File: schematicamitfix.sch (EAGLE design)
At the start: 39 parts, among them J1 FTDI_DEVICE, M1 WIRELESS-NRF24L01, U1 ATMEGA328P_TQFP, U2 GY-521MPU6050, U3 MAX1595EUA33+, Y1 8MHz

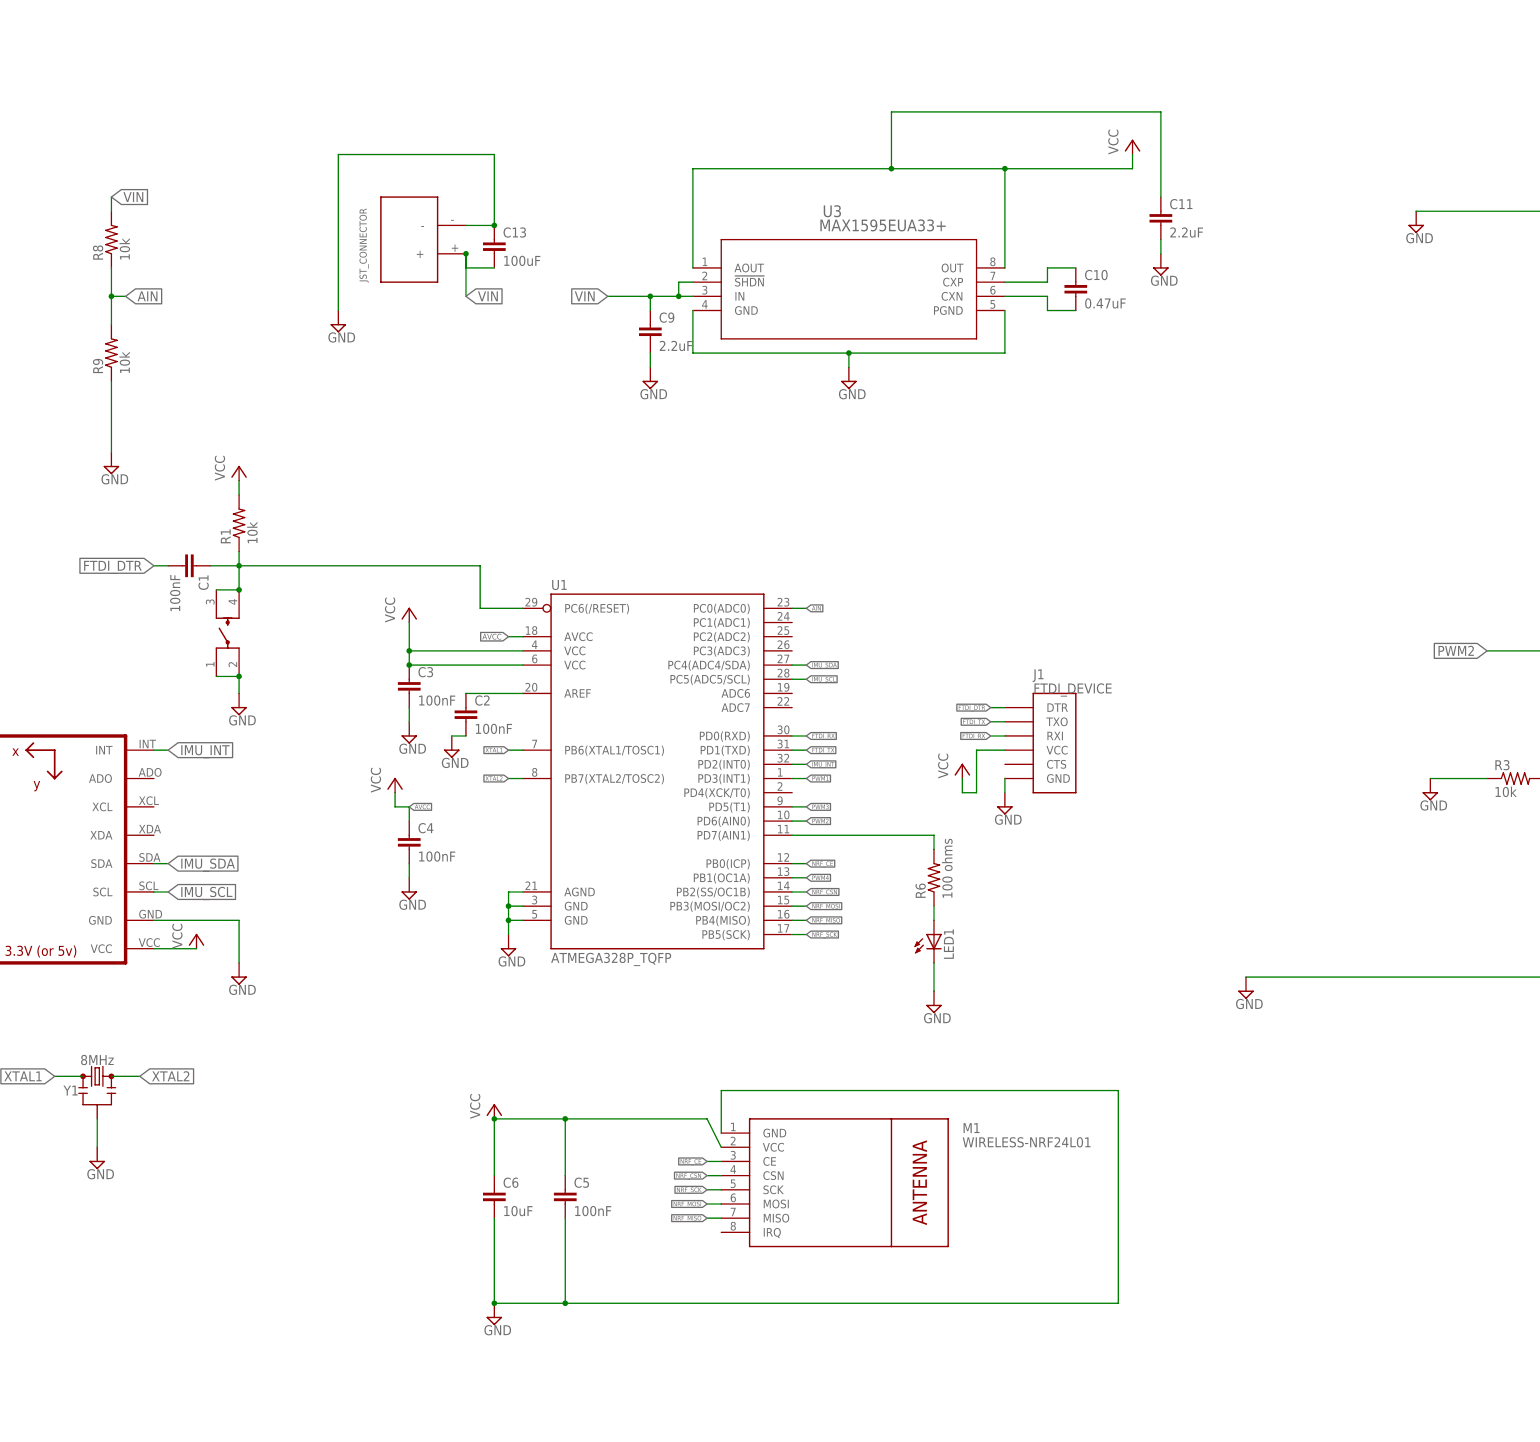
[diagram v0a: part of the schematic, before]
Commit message: Fixed ERC warnings about VCC and GND
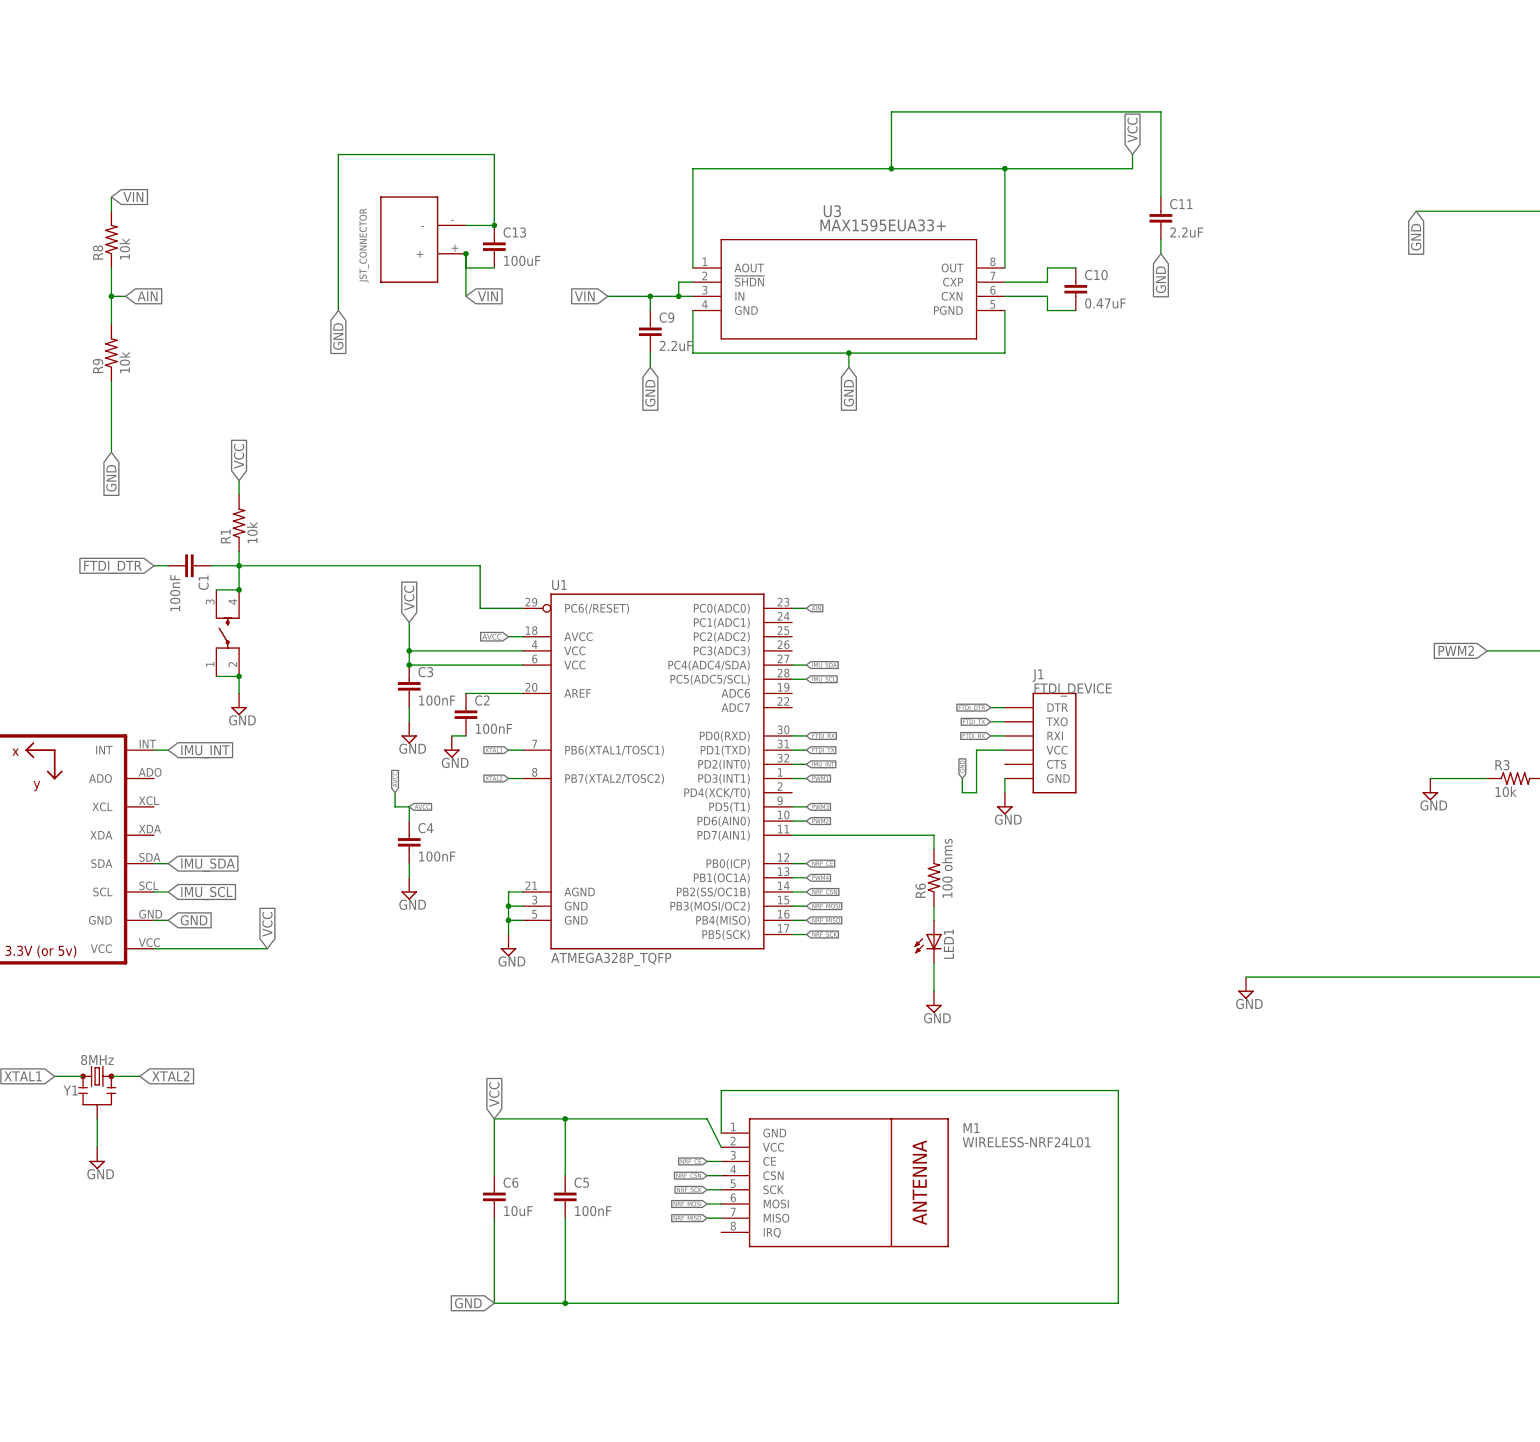
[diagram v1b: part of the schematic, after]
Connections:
- net GND: now also J1.VCC
- net VCC: no longer J1.VCC

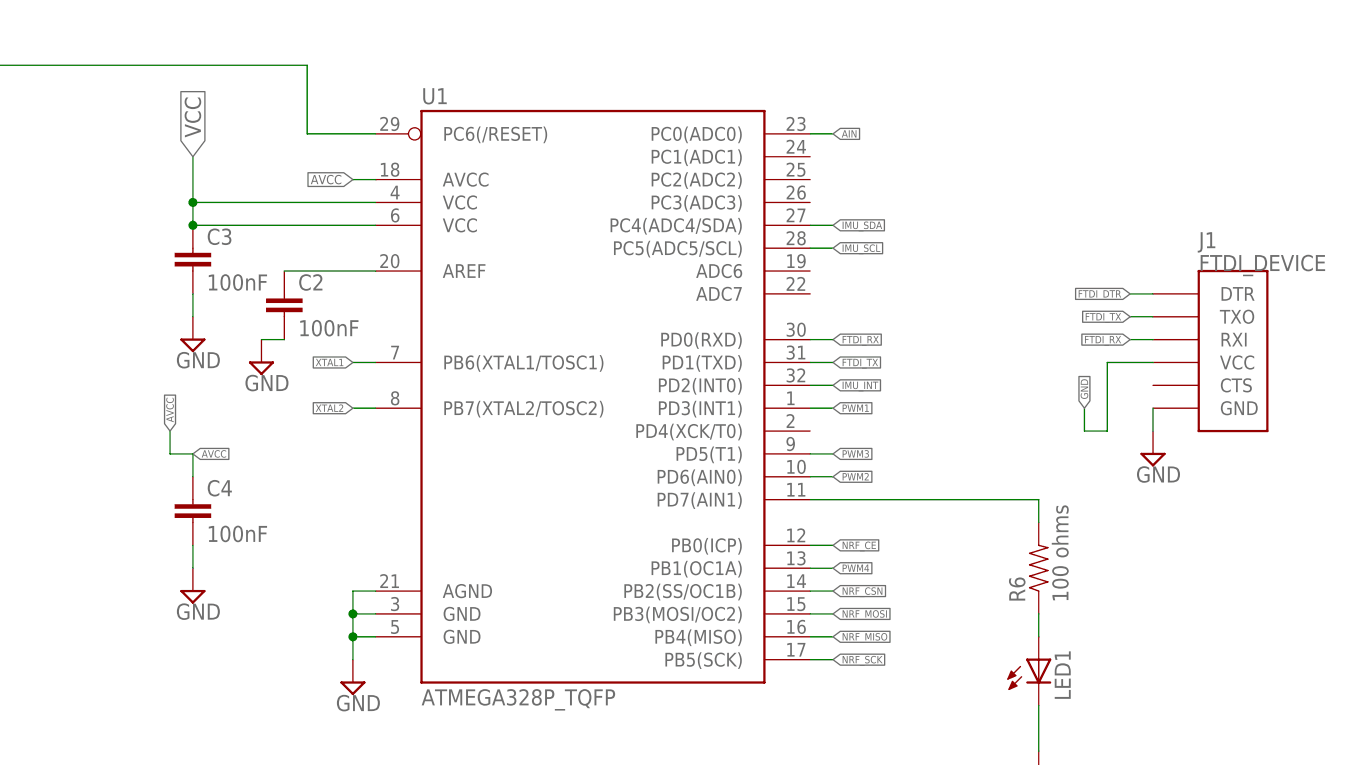
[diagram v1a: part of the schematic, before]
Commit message: Modified LED Resistor value
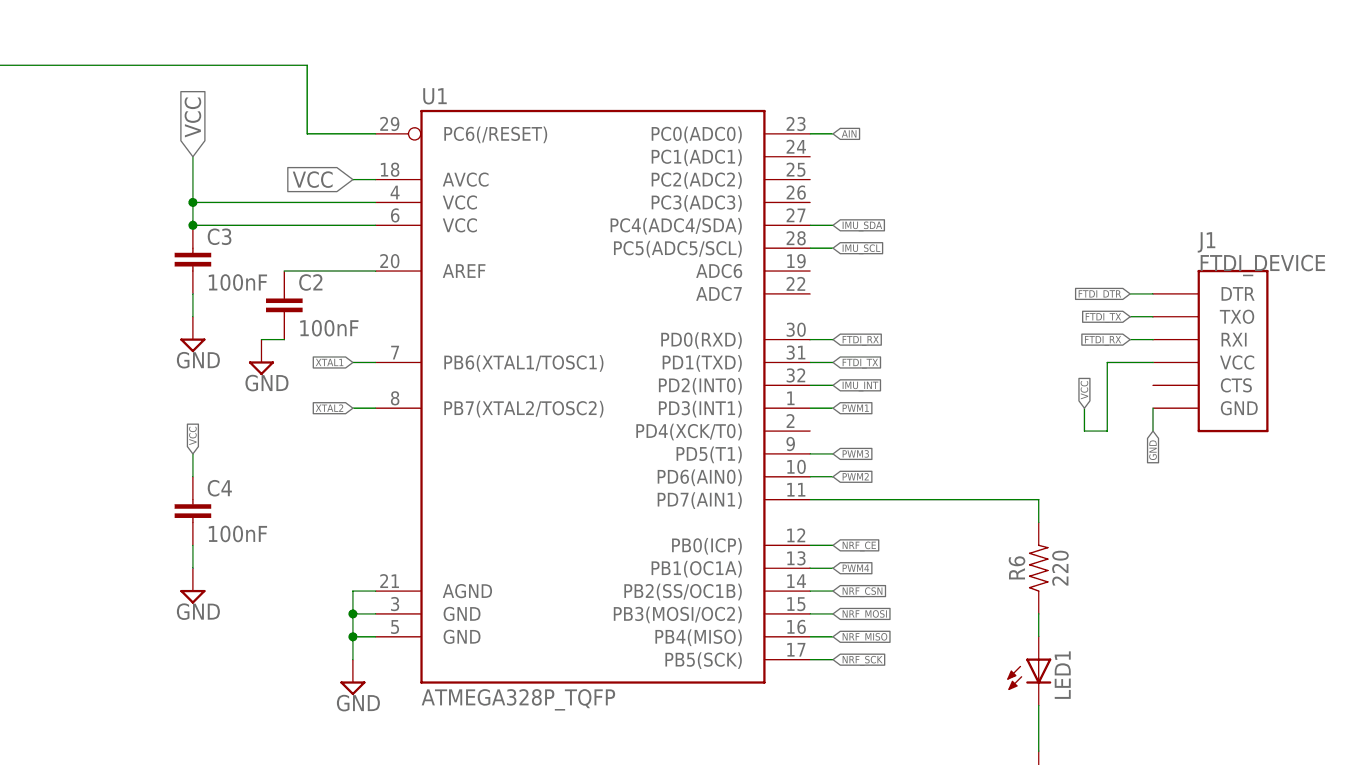
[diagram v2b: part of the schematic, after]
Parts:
- R6: value 100 ohms -> 220; device SparkFun:RESISTOR0603-RES -> SparkFun-Resistors:220OHM-0603-1/10W-1%
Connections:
- removed net AVCC: C4.1, U1.AVCC
- net GND: no longer J1.VCC
- net VCC: now also C4.1, J1.VCC, U1.AVCC
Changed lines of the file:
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@@
 <part name="U2" library="quad" deviceset="GY-521" device="MPU6050"/>
 <part name="M1" library="quad" deviceset="WIRELESS-NRF24L01" device=""/>
-<part name="SUPPLY2" library="supply2" library_urn="urn:adsk.eagle:library:372" deviceset="GND" device=""/>
 <part name="SUPPLY5" library="supply2" library_urn="urn:adsk.eagle:library:372" deviceset="GND" device=""/>
 <part name="SUPPLY6" library="supply2" library_urn="urn:adsk.eagle:library:372" deviceset="GND" device=""/>
@@
 <part name="R5" library="SparkFun-Resistors" deviceset="RESISTOR" device="0603" value="10k"/>
 <part name="LED1" library="LilyPad-Wearables" deviceset="LED" device="1206"/>
-<part name="R6" library="SparkFun" deviceset="RESISTOR" device="0603-RES" value="100 ohms"/>
 <part name="U$19" library="quad" deviceset="JST_CONNECTOR_FEMALE" device=""/>
 <part name="SUPPLY16" library="supply2" library_urn="urn:adsk.eagle:library:372" deviceset="GND" device=""/>
@@
 <part name="Y1" library="SparkFun-Clocks" deviceset="RESONATOR-8MHZ" device="SMD_3.2X1.3" value="8MHz"/>
 <part name="SUPPLY13" library="supply2" library_urn="urn:adsk.eagle:library:372" deviceset="GND" device=""/>
+<part name="R6" library="SparkFun-Resistors" deviceset="220OHM" device="-0603-1/10W-1%" value="220"/>
 </parts>
 <sheets>
@@
 <instance part="U2" gate="G$1" x="-43.18" y="22.86" rot="R180"/>
 <instance part="M1" gate="G$1" x="96.52" y="-35.56"/>
-<instance part="SUPPLY2" gate="GND" x="124.46" y="33.02"/>
 <instance part="SUPPLY5" gate="GND" x="35.56" y="7.62"/>
 <instance part="SUPPLY6" gate="GND" x="25.4" y="43.18"/>
@@
 <instance part="R5" gate="G$1" x="185.42" y="-254" rot="R90"/>
 <instance part="LED1" gate="G$1" x="111.76" y="10.16"/>
-<instance part="R6" gate="G$1" x="111.76" y="20.32" rot="R90"/>
 <instance part="U$19" gate="G$1" x="17.78" y="134.62" rot="R90"/>
 <instance part="SUPPLY16" gate="GND" x="264.16" y="236.22"/>
@@
 <instance part="Y1" gate="G$1" x="-38.1" y="-15.24"/>
 <instance part="SUPPLY13" gate="GND" x="-38.1" y="-30.48"/>
+<instance part="R6" gate="G$1" x="111.76" y="20.32" rot="R90"/>
 </instances>
 <busses>
@@
 </segment>
 <segment>
-<pinref part="J1" gate="G$1" pin="GND"/>
-<wire x1="124.46" y1="38.1" x2="124.46" y2="35.56" width="0.1524" layer="91"/>
-<pinref part="SUPPLY2" gate="GND" pin="GND"/>
-</segment>
-<segment>
 <wire x1="60.96" y1="114.3" x2="60.96" y2="111.76" width="0.1524" layer="91"/>
 <pinref part="C9" gate="G$1" pin="2"/>
@@
 </segment>
 <segment>
-<pinref part="J1" gate="G$1" pin="VCC"/>
-<wire x1="124.46" y1="43.18" x2="119.38" y2="43.18" width="0.1524" layer="91"/>
-<wire x1="119.38" y1="43.18" x2="119.38" y2="35.56" width="0.1524" layer="91"/>
-<wire x1="119.38" y1="35.56" x2="116.84" y2="35.56" width="0.1524" layer="91"/>
-<wire x1="116.84" y1="35.56" x2="116.84" y2="38.1" width="0.1524" layer="91"/>
-<label x="116.84" y="38.1" size="0.8128" layer="95" rot="R90" xref="yes"/>
+<pinref part="J1" gate="G$1" pin="GND"/>
+<wire x1="124.46" y1="38.1" x2="124.46" y2="35.56" width="0.1524" layer="91"/>
+<label x="124.46" y="35.56" size="0.8128" layer="95" rot="R270" xref="yes"/>
 </segment>
 </net>
@@
 <wire x1="-27.94" y1="7.62" x2="-7.62" y2="7.62" width="0.1524" layer="91"/>
 <label x="-7.62" y="7.62" size="1.778" layer="95" rot="R90" xref="yes"/>
-</segment>
-<segment>
-<pinref part="U1" gate="U$1" pin="VCC@6"/>
-<wire x1="38.1" y1="58.42" x2="17.78" y2="58.42" width="0.1524" layer="91"/>
-<pinref part="U1" gate="U$1" pin="VCC@4"/>
-<wire x1="38.1" y1="60.96" x2="17.78" y2="60.96" width="0.1524" layer="91"/>
-<wire x1="17.78" y1="58.42" x2="17.78" y2="60.96" width="0.1524" layer="91"/>
-<junction x="17.78" y="60.96"/>
-<wire x1="17.78" y1="60.96" x2="17.78" y2="66.04" width="0.1524" layer="91"/>
-<pinref part="C3" gate="G$1" pin="1"/>
-<junction x="17.78" y="58.42"/>
-<label x="17.78" y="66.04" size="1.778" layer="95" rot="R90" xref="yes"/>
 </segment>
 <segment>
@@
 <label x="147.32" y="149.86" size="1.778" layer="95" rot="R90" xref="yes"/>
 </segment>
+<segment>
+<pinref part="U1" gate="U$1" pin="VCC@6"/>
+<wire x1="38.1" y1="58.42" x2="17.78" y2="58.42" width="0.1524" layer="91"/>
+<pinref part="U1" gate="U$1" pin="VCC@4"/>
+<wire x1="38.1" y1="60.96" x2="17.78" y2="60.96" width="0.1524" layer="91"/>
+<wire x1="17.78" y1="58.42" x2="17.78" y2="60.96" width="0.1524" layer="91"/>
+<junction x="17.78" y="60.96"/>
+<wire x1="17.78" y1="60.96" x2="17.78" y2="66.04" width="0.1524" layer="91"/>
+<pinref part="C3" gate="G$1" pin="1"/>
+<junction x="17.78" y="58.42"/>
+<label x="17.78" y="66.04" size="1.778" layer="95" rot="R90" xref="yes"/>
+</segment>
+<segment>
+<pinref part="U1" gate="U$1" pin="AVCC"/>
+<wire x1="38.1" y1="63.5" x2="35.56" y2="63.5" width="0.1524" layer="91"/>
+<label x="35.56" y="63.5" size="1.778" layer="95" rot="R180" xref="yes"/>
+</segment>
+<segment>
+<pinref part="C4" gate="G$1" pin="1"/>
+<wire x1="17.78" y1="30.48" x2="17.78" y2="33.02" width="0.1524" layer="91"/>
+<label x="17.78" y="33.02" size="0.8128" layer="95" rot="R90" xref="yes"/>
+</segment>
+<segment>
+<pinref part="J1" gate="G$1" pin="VCC"/>
+<wire x1="124.46" y1="43.18" x2="119.38" y2="43.18" width="0.1524" layer="91"/>
+<wire x1="119.38" y1="43.18" x2="119.38" y2="35.56" width="0.1524" layer="91"/>
+<wire x1="119.38" y1="35.56" x2="116.84" y2="35.56" width="0.1524" layer="91"/>
+<wire x1="116.84" y1="35.56" x2="116.84" y2="38.1" width="0.1524" layer="91"/>
+<label x="116.84" y="38.1" size="0.8128" layer="95" rot="R90" xref="yes"/>
+</segment>
 </net>
 <net name="FTDI_TX" class="0">
@@
 </segment>
 </net>
-<net name="AVCC" class="0">
-<segment>
-<pinref part="U1" gate="U$1" pin="AVCC"/>
-<wire x1="38.1" y1="63.5" x2="35.56" y2="63.5" width="0.1524" layer="91"/>
-<label x="35.56" y="63.5" size="1.016" layer="95" rot="R180" xref="yes"/>
-</segment>
-<segment>
-<pinref part="C4" gate="G$1" pin="1"/>
-<wire x1="17.78" y1="30.48" x2="17.78" y2="33.02" width="0.1524" layer="91"/>
-<label x="17.78" y="33.02" size="0.8128" layer="95" xref="yes"/>
-<wire x1="17.78" y1="33.02" x2="15.24" y2="33.02" width="0.1524" layer="91"/>
-<wire x1="15.24" y1="33.02" x2="15.24" y2="35.56" width="0.1524" layer="91"/>
-<label x="15.24" y="35.56" size="0.8128" layer="95" rot="R90" xref="yes"/>
-</segment>
-</net>
 <net name="PWM2" class="0">
 <segment>
@@
 <net name="N$7" class="0">
 <segment>
-<pinref part="R6" gate="G$1" pin="2"/>
 <wire x1="111.76" y1="27.94" x2="111.76" y2="25.4" width="0.1524" layer="91"/>
 <pinref part="U1" gate="U$1" pin="PD7(AIN1)"/>
 <wire x1="111.76" y1="27.94" x2="86.36" y2="27.94" width="0.1524" layer="91"/>
+<pinref part="R6" gate="G$1" pin="2"/>
 </segment>
 </net>
 <net name="N$11" class="0">
 <segment>
-<pinref part="R6" gate="G$1" pin="1"/>
 <pinref part="LED1" gate="G$1" pin="A"/>
 <wire x1="111.76" y1="15.24" x2="111.76" y2="12.7" width="0.1524" layer="91"/>
-</segment>
-</net>
+<pinref part="R6" gate="G$1" pin="1"/>
+</segment>
+</net>
